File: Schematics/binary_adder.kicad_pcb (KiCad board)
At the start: 2 copper layers, 97.7 x 50.6 mm, 32 parts, among them SW1 SW_Push, SW2 SW_Push, U1 4040, U2 LM555xN

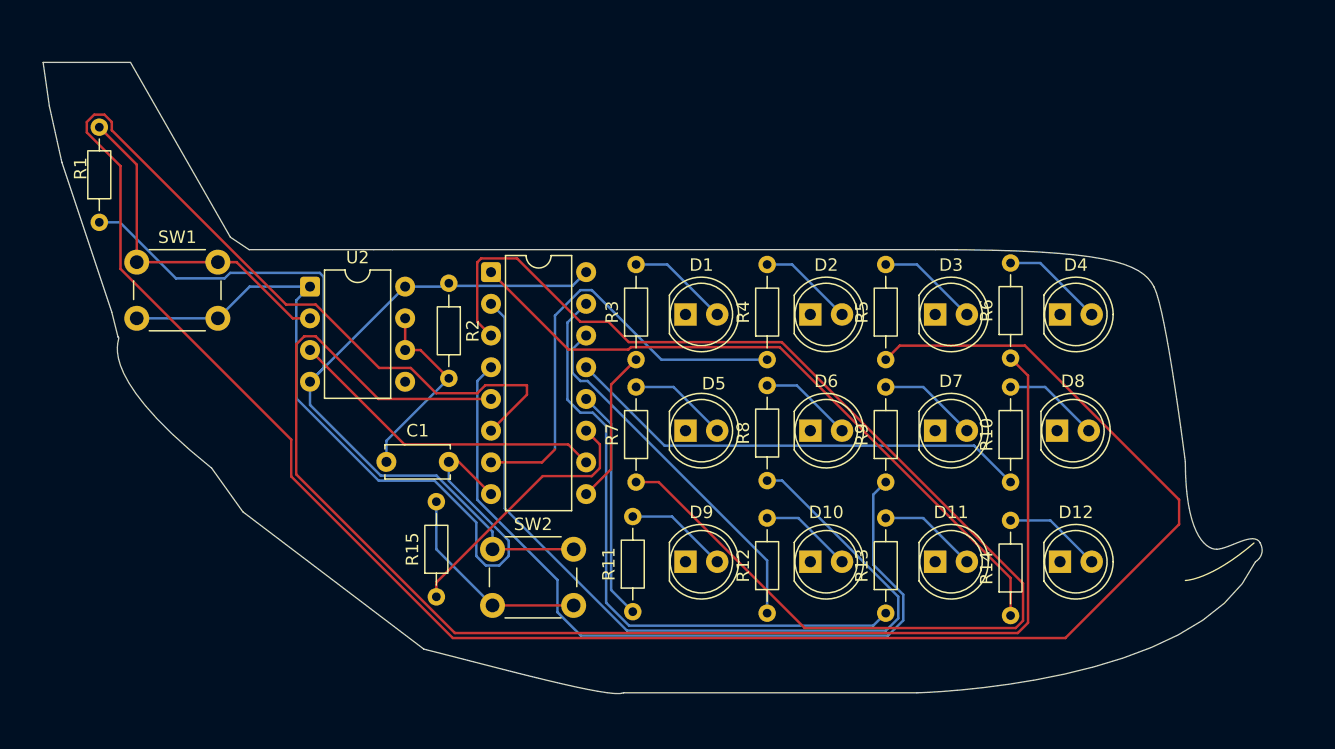
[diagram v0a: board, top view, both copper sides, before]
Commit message: Fix GND pull resistor in schematic
Also add ground pour
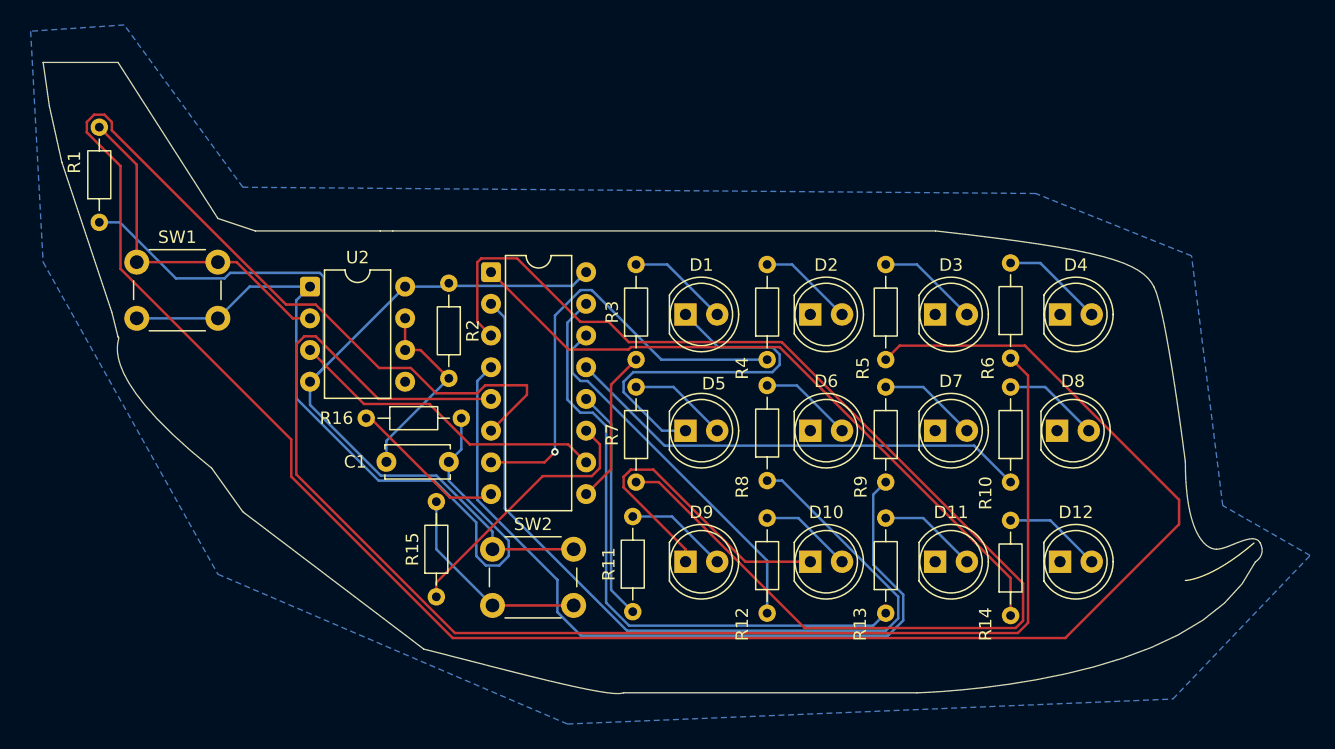
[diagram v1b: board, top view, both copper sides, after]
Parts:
- added R16: 10k, Resistor_THT:R_Axial_DIN0204_L3.6mm_D1.6mm_P7.62mm_Horizontal, F.Cu at (116.4, 101.5)
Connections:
- D1 pad 1: unconnected-(D1-K-Pad1) -> GND
- D10 pad 1: unconnected-(D10-K-Pad1) -> GND
- D11 pad 1: unconnected-(D11-K-Pad1) -> GND
- D12 pad 1: unconnected-(D12-K-Pad1) -> GND
- D2 pad 1: unconnected-(D2-K-Pad1) -> GND
- D3 pad 1: unconnected-(D3-K-Pad1) -> GND
- D4 pad 1: unconnected-(D4-K-Pad1) -> GND
- D5 pad 1: unconnected-(D5-K-Pad1) -> GND
- D6 pad 1: unconnected-(D6-K-Pad1) -> GND
- D7 pad 1: unconnected-(D7-K-Pad1) -> GND
- D8 pad 1: unconnected-(D8-K-Pad1) -> GND
- D9 pad 1: unconnected-(D9-K-Pad1) -> GND
- U1 pad 8: GND -> Net-(U1-VSS)
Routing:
- net GND: track 62.8 -> 119.2 mm
- net Net-(U1-VSS): track 0.00 -> 12.4 mm
- net /Q1: track 36.4 -> 36.3 mm, vias 0 -> 1
- added copper zone on B.Cu, net GND
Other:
- outline, holes or cut-outs redrawn

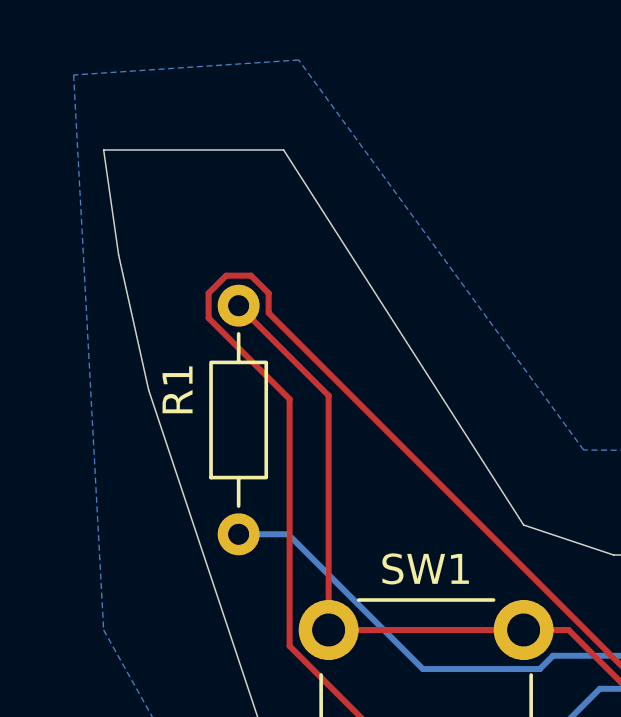
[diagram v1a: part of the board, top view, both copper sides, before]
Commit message: Add missing power connector
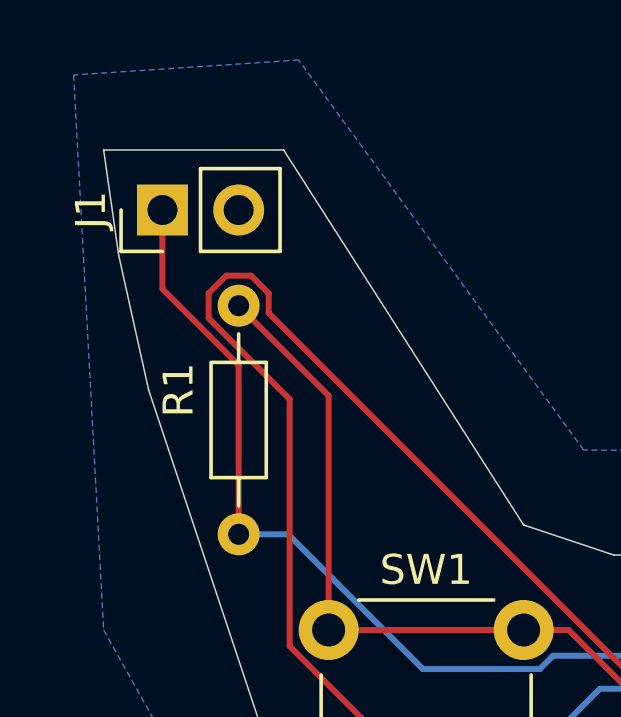
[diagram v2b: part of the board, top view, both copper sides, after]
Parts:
- added J1: Conn_01x02, Connector_PinHeader_2.54mm:PinHeader_1x02_P2.54mm_Vertical, F.Cu at (92.5, 75.0)
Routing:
- net VCC: track 83.5 -> 95.4 mm

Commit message: Change pull down resistor
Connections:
- R15 pad 2: Net-(R15-Pad2) -> GND
- SW2 pad 2: Net-(R15-Pad2) -> Net-(U1-Reset)
- U1 pad 8: Net-(U1-VSS) -> GND
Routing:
- net Net-(R15-Pad2): track 16.7 -> 0.00 mm
- net (no net): track 0.00 -> 16.7 mm
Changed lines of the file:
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@@
 	(net 31 "/Q11")
 	(net 32 "Net-(U1-Reset)")
-	(net 33 "Net-(R15-Pad2)")
 	(footprint "Resistor_THT:R_Axial_DIN0204_L3.6mm_D1.6mm_P7.62mm_Horizontal"
 		(layer "F.Cu")
@@
 			(layers "*.Cu" "*.Mask")
 			(remove_unused_layers no)
-			(net 33 "Net-(R15-Pad2)")
+			(net 4 "GND")
 			(pintype "passive")
 		)
@@
 			(layers "*.Cu" "*.Mask")
 			(remove_unused_layers no)
-			(net 8 "Net-(U1-VSS)")
+			(net 4 "GND")
 			(pinfunction "VSS")
 			(pintype "power_in")
@@
 			(layers "*.Cu" "*.Mask")
 			(remove_unused_layers no)
-			(net 33 "Net-(R15-Pad2)")
+			(net 32 "Net-(U1-Reset)")
 			(pinfunction "2")
 			(pintype "passive")
@@
 			(layers "*.Cu" "*.Mask")
 			(remove_unused_layers no)
-			(net 33 "Net-(R15-Pad2)")
+			(net 32 "Net-(U1-Reset)")
 			(pinfunction "2")
 			(pintype "passive")
@@
 	)
 	(segment
+		(start 126.5 116.5)
+		(end 133 116.5)
+		(width 0.2)
+		(layer "F.Cu")
+		(net 0)
+	)
+	(segment
+		(start 122 108.19)
+		(end 122 112)
+		(width 0.2)
+		(layer "B.Cu")
+		(net 0)
+	)
+	(segment
+		(start 122 112)
+		(end 126.5 116.5)
+		(width 0.2)
+		(layer "B.Cu")
+		(net 0)
+	)
+	(segment
 		(start 92.46 77.632728)
 		(end 95 80.172728)
@@
 		(net 32)
 	)
-	(segment
-		(start 126.5 116.5)
-		(end 133 116.5)
-		(width 0.2)
-		(layer "F.Cu")
-		(net 33)
-	)
-	(segment
-		(start 122 108.19)
-		(end 122 112)
-		(width 0.2)
-		(layer "B.Cu")
-		(net 33)
-	)
-	(segment
-		(start 122 112)
-		(end 126.5 116.5)
-		(width 0.2)
-		(layer "B.Cu")
-		(net 33)
-	)
 	(zone
